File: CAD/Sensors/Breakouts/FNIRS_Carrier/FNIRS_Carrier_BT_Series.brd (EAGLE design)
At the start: 99.8 x 53.2 mm, 36 parts, among them J1 62202021121, J2 62202021121, J3 20021111-00016T4LF, J4 20021111-00016T4LF, J5 20021111-00016T4LF, X1 TSW-108-07-G-S

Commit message: edit
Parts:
- moved J3 1.44 mm to (1.80, 30.8)
- moved J5 1.44 mm to (-20.7, 25.1)
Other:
- board size 99.8 x 53.2 mm -> 100.8 x 54.2 mm

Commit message: add
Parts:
- moved J4 6.68 mm to (-33.4, 40.4)
- moved J3 4.02 mm to (5.11, 33.1)
- moved J5 2.67 mm to (-22.9, 23.7)
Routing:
- net GND: track 552.8 -> 621.0 mm
- net AOUT6_5P: track 85.9 -> 78.8 mm
- net 4P: track 43.2 -> 50.3 mm
- net 2P: track 39.4 -> 46.5 mm
- net 0P: track 28.3 -> 35.4 mm
- net 3P: track 43.7 -> 50.8 mm
- net AOUT8_7P: track 79.8 -> 72.7 mm
- net AOUT7_6P: track 83.0 -> 75.9 mm
- net AOUT5_4P: track 88.8 -> 81.7 mm
- net AOUT4_3P: track 85.4 -> 78.3 mm
- net AOUT3_2P: track 88.8 -> 81.7 mm
- net 6P: track 35.1 -> 42.2 mm
- net 5P: track 39.2 -> 46.3 mm
- net 1P: track 35.0 -> 42.1 mm
- net 7P: track 28.7 -> 35.8 mm
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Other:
- board size 100.8 x 54.2 mm -> 103.9 x 55.4 mm

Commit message: modifed io order on bt840, some nrf52840 firmware cleanup (need to update with compass and audio too)
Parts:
- moved J5 36.9 mm to (10.0, 40.3), flipped to the bottom, turned to 0 degrees
- moved J2 27.1 mm to (-2.03, 61.4), turned to 90 degrees
- moved J1 21.7 mm to (-26.4, 60.8), turned to 90 degrees
- moved J3 19.3 mm to (-14.1, 30.8), flipped to the top, turned to 180 degrees
- moved J4 3.05 mm to (-36.5, 40.6)
- moved U$1 2.41 mm to (-41.0, 60.8)
- moved R2 1.53 mm to (-46.5, 54.5)
- moved R3 1.53 mm to (-46.5, 56.7)
- moved R6 1.53 mm to (-46.5, 63.5)
- moved R1 1.53 mm to (-46.5, 52.2)
- moved R7 1.53 mm to (-46.5, 65.7)
- moved R4 1.53 mm to (-46.5, 59.1)
- moved R17 1.53 mm to (-46.4, 70.1)
- moved R18 1.53 mm to (-46.4, 72.3)
- moved R5 1.53 mm to (-46.5, 61.2)
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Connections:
- new net P28_AIN1: J2.8
- new net P29_AIN1: J2.4
- new net P30_AIN1: J2.7
- net CLKOUT: now also J1.20; no longer J1.10
- net CS: now also J1.18; no longer J1.8
- net DCCH: now also J2.1; no longer J2.11
- net DIN: now also J1.19; no longer J1.9
- net DOUT: now also J1.4; no longer J1.14
- net DRDY: now also J1.16; no longer J1.6
- net GND: now also J2.19; no longer J2.9
- net MAX_INT: now also J1.5; no longer J1.15
- net MPU_INT: now also J1.3; no longer J1.13
- net P100: now also J2.17; no longer J2.7
- net P106: now also J1.14; no longer J1.4
- net P107: now also J2.2; no longer J2.12
- net P109: now also J2.11; no longer J2.1
- net P11: now also J2.18; no longer J2.8
- net P110: now also J1.12; no longer J1.2
- net P111: now also J2.10; no longer J2.20
- net P112: now also J2.9; no longer J2.19
- net P113: now also J1.10; no longer J1.20
- net P114: now also J1.8; no longer J1.18
- net P12: now also J2.12; no longer J2.2
- net P13: now also J2.16; no longer J2.6
- net P17: now also J2.6; no longer J2.16
- net P22: now also J2.5; no longer J2.15
- net P24: now also J2.3; no longer J2.13
- net P26_SDA: now also J1.7; no longer J1.17
- net P27_SCL: now also J1.6; no longer J1.16
- net P28_AIN4: no longer J2.18
- net P29_AIN5: no longer J2.14
- net P30_AIN6: no longer J2.17
- net P31_AIN7: now also J1.11; no longer J1.1
- net P3_AIN1: now also J1.2; no longer J1.12
- net P4_AIN2: now also J1.9; no longer J1.19
- net P5_AIN3: now also J1.1; no longer J1.11
- net P7: now also J1.13; no longer J1.3
- net RESET: now also J2.15; no longer J2.5
- net SCLK: now also J1.17; no longer J1.7
- net SWDCLK: now also J2.14; no longer J2.4
- net SWDIO: now also J2.13; no longer J2.3
- net SYNC/RESET: now also J1.15; no longer J1.5
- net VDD: now also J2.20; no longer J2.10
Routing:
- net GND: track 621.0 -> 305.5 mm, vias 4 -> 2
- net CLKOUT: track 70.4 -> 14.7 mm, vias 1 -> 0
- net SCLK: track 54.6 -> 0.74 mm
- net SYNC/RESET: track 53.1 -> 0.00 mm, vias 2 -> 0
- net DRDY: track 52.6 -> 0.64 mm, vias 2 -> 0
- net 3P: track 50.8 -> 0.00 mm
- net CS: track 55.8 -> 5.11 mm
- net 4P: track 50.3 -> 0.00 mm
- net DIN: track 59.3 -> 9.55 mm, vias 1 -> 0
- net P114: track 63.1 -> 15.2 mm, vias 3 -> 0
- net 2P: track 46.5 -> 0.00 mm
- net 5P: track 46.3 -> 0.00 mm
- net DOUT: track 52.1 -> 6.52 mm
- net P4_AIN2: track 59.4 -> 15.6 mm, vias 3 -> 0
- net 6P: track 42.2 -> 0.00 mm
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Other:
- board size 103.9 x 55.4 mm -> 98.3 x 37.7 mm
- board text removed: "Microcontroller faces back and attaches from this side (front)"

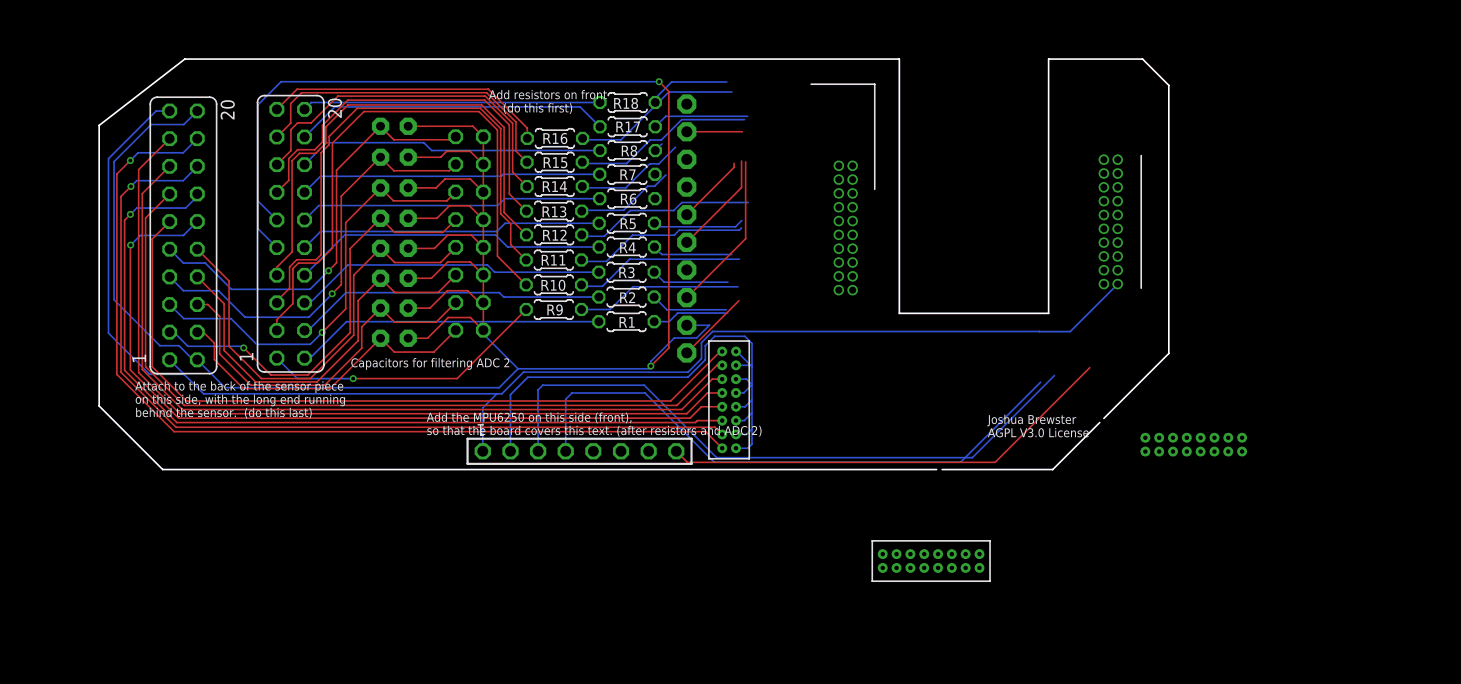
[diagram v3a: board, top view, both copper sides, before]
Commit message: fixed fnirs carrier board
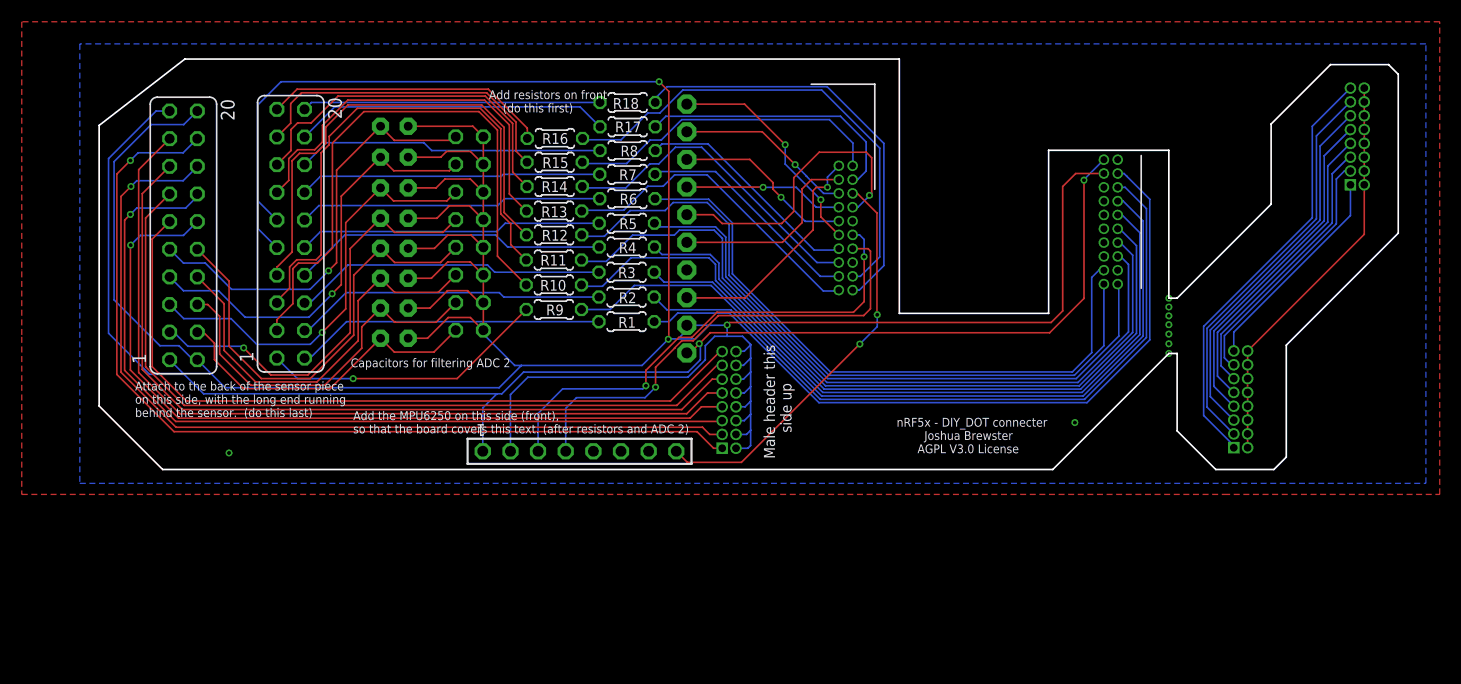
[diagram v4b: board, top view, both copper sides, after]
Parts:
- removed J3, J4, J5: 20021111-00016T4LF, 2x8_1.27mm:CONN16_016T4LF_AMP
- added J6, J7, J8: FTSH-108-02-LM-D-ES, 16pos1.27mm:SAMTEC_FTSH-108-02-LM-D-ES
- turned J1 to 270 degrees
- turned J2 to 270 degrees
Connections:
- removed net 0P: J3.2, J5.2
- removed net 1P: J3.4, J5.4
- removed net 2P: J3.6, J5.6
- removed net 3P: J3.8, J5.8
- removed net 4P: J3.10, J5.10
- removed net 5P: J3.12, J5.12
- removed net 6P: J3.14, J5.14
- removed net 7P: J3.16, J5.16
- removed net P28_AIN1: J2.8
- removed net P28_AIN4: R8.1
- removed net P29_AIN1: J2.4
- removed net P29_AIN5: R4.1
- removed net P30_AIN1: J2.7
- removed net P30_AIN6: R7.1
- new net P28_AIN: J2.8, R11.1
- new net P29_AIN: J2.4, R9.1
- new net P30_AIN: J2.7, R4.1
- net AOUT1_0P: now also J6.01, J7.01, J8.15; no longer J4.2
- net AOUT2_1P: now also J6.03, J7.03, J8.13; no longer J4.4
- net AOUT3_2P: now also J6.05, J7.05, J8.11; no longer J4.6
- net AOUT4_3P: now also J6.07, J7.07, J8.09; no longer J4.8
- net AOUT5_4P: now also J6.09, J7.09, J8.07; no longer J4.10
- net AOUT6_5P: now also J6.11, J7.11, J8.05; no longer J4.12
- net AOUT7_6P: now also J6.13, J7.13, J8.03; no longer J4.14
- net AOUT8_7P: now also J6.15, J7.15, J8.01; no longer J4.16
- net GND: now also J6.02, J6.04, J6.06, J6.08, J6.10, J6.12, J6.14, J6.16, J7.02, J7.04, J7.06, J7.08, J7.10, J7.12, J7.14, J7.16, J8.02, J8.04, J8.06, J8.08, J8.10, J8.12, J8.14, J8.16; no longer J3.1, J3.11, J3.13, J3.15, J3.3, J3.5, J3.7, J3.9, J4.1, J4.11, J4.13, J4.15, J4.3, J4.5, J4.7, J4.9, J5.1, J5.11, J5.13, J5.15, J5.3, J5.5, J5.7, J5.9
- net P100: no longer R13.1
- net P106: now also R8.1
- net P107: now also R1.1; no longer R2.1
- net P109: now also R12.1; no longer R16.1
- net P11: no longer R1.1
- net P110: now also R7.1
- net P111: now also R5.1; no longer R18.1
- net P112: no longer R17.1
- net P113: now also R18.1; no longer R11.1
- net P114: no longer R9.1
- net P12: now also R6.1; no longer R15.1
- net P13: no longer R14.1
- net P17: now also R10.1; no longer R6.1
- net P22: now also R3.1; no longer R5.1
- net P24: now also R2.1; no longer R3.1
- net P31_AIN7: now also R13.1; no longer R12.1
- net P3_AIN1: now also R17.1
- net P4_AIN2: now also R16.1; no longer R10.1
- net P5_AIN3: now also R15.1
- net P7: now also R14.1
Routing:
- net GND: track 305.5 -> 389.6 mm, vias 2 -> 5
- net P29_AIN: track 0.00 -> 72.7 mm
- net P17: track 0.05 -> 70.5 mm
- net P28_AIN: track 0.00 -> 68.9 mm
- net P107: track 7.11 -> 68.5 mm
- net P30_AIN: track 0.00 -> 61.1 mm
- net P24: track 7.16 -> 66.8 mm
- net P22: track 8.41 -> 63.5 mm
- net P109: track 15.6 -> 65.4 mm
- net P111: track 7.58 -> 57.2 mm
- net P12: track 16.6 -> 58.5 mm
- net AOUT1_0P: track 85.6 -> 125.4 mm
- net AOUT2_1P: track 81.9 -> 118.9 mm
- net AOUT3_2P: track 78.6 -> 112.7 mm
- net AOUT4_3P: track 75.1 -> 106.5 mm
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- added copper zone on layer 1, net GND
- added copper zone on layer 16, net GND
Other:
- board size 98.3 x 37.7 mm -> 119.4 x 37.7 mm
- board text added: "Female headers this side, facing back"
- board text added: "Male header this side up"
- board text added: "nRF5x - DIY_DOT connecter Joshua Brewster AGPL V3.0 License"
- board text removed: "Joshua Brewster AGPL V3.0 License"
